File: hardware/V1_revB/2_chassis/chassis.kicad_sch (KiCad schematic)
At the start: 18 parts, among them SW3 NKK_NR01

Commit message: Feat(Hw):Modify_footprint_Chasis_Pot
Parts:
- removed RV3: R_POT_TRIM_US, Global_Library:POT_ECU, symbol Device:R_POT_TRIM_US
- added RV1: R_Potentiometer, RAMN_New_Footprint:New_Pot, symbol Device:R_Potentiometer
- J7, SW2: value ~ -> (none)
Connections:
- net 3V3_ECU: now also RV1.3
- net GND: now also RV1.1
- net Wheel: now also RV1.2

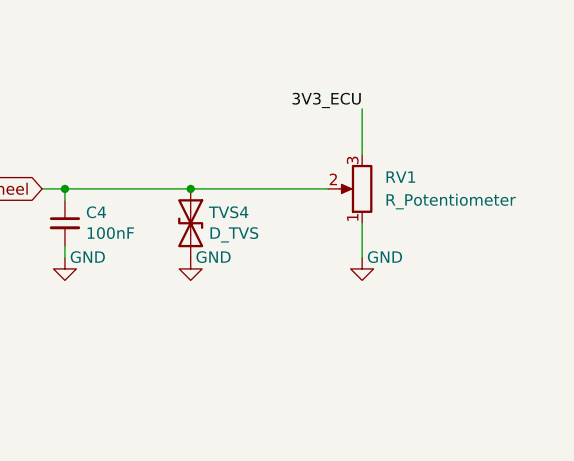
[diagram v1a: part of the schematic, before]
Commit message: Feat(Hw):Modify_BOM_LCSC#
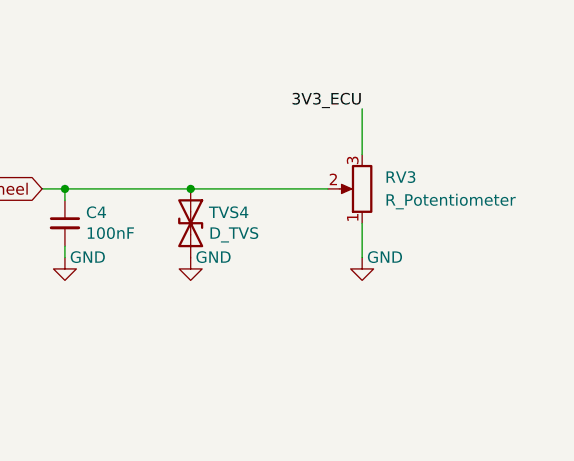
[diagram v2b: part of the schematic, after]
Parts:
- C4: LCSC (none) -> C282519
- J7: LCSC (none) -> C2897414
- R10, R11, R7, R8, R9: LCSC (none) -> C73809
- RV3: renamed from RV1; LCSC (none) -> C6139964
- SW2: LCSC (none) -> C226259
- SW3: LCSC (none) -> C7250022
- TVS4, TVS5, TVS6: LCSC (none) -> C1849694
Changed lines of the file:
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@@
+			)
+		)
+		(property "LCSC" "C226259"
+			(at 128.27 160.02 0)
+			(hide yes)
+			(show_name no)
+			(do_not_autoplace no)
+			(effects
+				(font
+					(size 1.27 1.27)
+				)
 			)
 		)
@@
 			)
 		)
+		(property "LCSC" "C2897414"
+			(at 93.98 68.58 0)
+			(hide yes)
+			(show_name no)
+			(do_not_autoplace no)
+			(effects
+				(font
+					(size 1.27 1.27)
+				)
+			)
+		)
 		(pin "10"
 		)
@@
 		(property "Reference" "SW3"
 			(at 113.03 104.775 0)
-			(show_name no)
+			(show_name yes)
 			(do_not_autoplace no)
 			(effects
@@
 			)
 		)
-		(property "Datasheet" ""
+		(property "Datasheet" "https://www.lcsc.com/datasheet/C7250022.pdf?spm=wm.sxq.inf.ggs&lcsc_vid=FVIIUAUFR1ZWVAJSRgQLVgVfRwNWBVwDR1VbBFNeQ1ExVlNeQFFWV1FSQ1FYUDsOAxUeFF5JWBYZEEoKFBINSQcJGk4eFQsCAgIaSgADAwAHC0slRFVdUVZeQllADxALGw%3D%3D"
 			(at 112.395 113.665 0)
 			(hide yes)
@@
 		)
 		(property "Description" ""
+			(at 113.03 114.3 0)
+			(hide yes)
+			(show_name no)
+			(do_not_autoplace no)
+			(effects
+				(font
+					(size 1.27 1.27)
+				)
+			)
+		)
+		(property "LCSC" "C7250022"
 			(at 113.03 114.3 0)
 			(hide yes)
@@
 			)
 		)
+		(property "LCSC" ""
+			(at 26.67 44.45 0)
+			(hide yes)
+			(show_name no)
+			(do_not_autoplace no)
+			(effects
+				(font
+					(size 1.27 1.27)
+				)
+			)
+		)
 		(instances
 			(project "chassis"
@@
 			)
 		)
+		(property "LCSC" "C73809"
+			(at 96.52 105.41 0)
+			(hide yes)
+			(show_name no)
+			(do_not_autoplace no)
+			(effects
+				(font
+					(size 1.27 1.27)
+				)
+			)
+		)
 		(pin "1"
 		)
@@
 			)
 		)
+		(property "LCSC" "C73809"
+			(at 96.52 114.3 0)
+			(hide yes)
+			(show_name no)
+			(do_not_autoplace no)
+			(effects
+				(font
+					(size 1.27 1.27)
+				)
+			)
+		)
 		(pin "2"
 		)
@@
 			)
 		)
+		(property "LCSC" "C73809"
+			(at 96.52 120.65 0)
+			(hide yes)
+			(show_name no)
+			(do_not_autoplace no)
+			(effects
+				(font
+					(size 1.27 1.27)
+				)
+			)
+		)
 		(pin "2"
 		)
@@
 			)
 		)
+		(property "LCSC" "C73809"
+			(at 96.52 128.27 0)
+			(hide yes)
+			(show_name no)
+			(do_not_autoplace no)
+			(effects
+				(font
+					(size 1.27 1.27)
+				)
+			)
+		)
 		(pin "2"
 		)
@@
 			)
 		)
+		(property "LCSC" "C73809"
+			(at 119.38 154.94 0)
+			(hide yes)
+			(show_name no)
+			(do_not_autoplace no)
+			(effects
+				(font
+					(size 1.27 1.27)
+				)
+			)
+		)
 		(pin "1"
 		)
@@
 			)
 		)
+		(property "LCSC" ""
+			(at 26.67 39.37 0)
+			(hide yes)
+			(show_name no)
+			(do_not_autoplace no)
+			(effects
+				(font
+					(size 1.27 1.27)
+				)
+			)
+		)
 		(instances
 			(project "chassis"
@@
 			)
 		)
+		(property "LCSC" "C282519"
+			(at 137.16 59.69 0)
+			(hide yes)
+			(show_name no)
+			(do_not_autoplace no)
+			(effects
+				(font
+					(size 1.27 1.27)
+				)
+			)
+		)
 		(pin "1"
 		)
@@
 			)
 		)
+		(property "LCSC" "C1849694"
+			(at 151.13 59.69 90)
+			(hide yes)
+			(show_name no)
+			(do_not_autoplace no)
+			(effects
+				(font
+					(size 1.27 1.27)
+				)
+			)
+		)
 		(pin "1"
 		)
@@
 			)
 		)
+		(property "LCSC" "C1849694"
+			(at 130.81 119.38 90)
+			(hide yes)
+			(show_name no)
+			(do_not_autoplace no)
+			(effects
+				(font
+					(size 1.27 1.27)
+				)
+			)
+		)
 		(pin "2"
 		)
@@
 			)
 		)
+		(property "LCSC" "C1849694"
+			(at 115.57 165.1 90)
+			(hide yes)
+			(show_name no)
+			(do_not_autoplace no)
+			(effects
+				(font
+					(size 1.27 1.27)
+				)
+			)
+		)
 		(pin "1"
 		)
@@
 			)
 		)
+		(property "LCSC" ""
+			(at 25.4 176.53 0)
+			(hide yes)
+			(show_name no)
+			(do_not_autoplace no)
+			(effects
+				(font
+					(size 1.27 1.27)
+				)
+			)
+		)
 		(instances
 			(project "chassis"
@@
 			)
 		)
+		(property "LCSC" ""
+			(at 41.91 176.53 0)
+			(hide yes)
+			(show_name no)
+			(do_not_autoplace no)
+			(effects
+				(font
+					(size 1.27 1.27)
+				)
+			)
+		)
 		(instances
 			(project "chassis"
@@
 			)
 		)
+		(property "LCSC" ""
+			(at 58.42 176.53 0)
+			(hide yes)
+			(show_name no)
+			(do_not_autoplace no)
+			(effects
+				(font
+					(size 1.27 1.27)
+				)
+			)
+		)
 		(instances
 			(project "chassis"
@@
 		(in_pos_files yes)
 		(dnp no)
-		(property "Reference" "RV1"
+		(property "Reference" "RV3"
 			(at 172.72 54.6099 0)
 			(show_name no)
@@
 			)
 		)
+		(property "LCSC" "C6139964"
+			(at 170.18 55.88 0)
+			(hide yes)
+			(show_name no)
+			(do_not_autoplace no)
+			(effects
+				(font
+					(size 1.27 1.27)
+				)
+			)
+		)
 		(pin "2"
 		)
@@
 			(project "chassis"
 				(path "/e002719d-0ac0-46ab-ae27-c279a7634c07"
-					(reference "RV1")
-					(unit 1)
-				)
+					(reference "RV3")
+					(unit 1)
+				)

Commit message: Feat(Hw): Modify_and_fix_footprints_and_symbols
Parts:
- removed SW3: NKK_NR01, Akiyuki_UI:NR01, symbol Akiyuki_UI:NKK_NR01
- added SW1: (no value), RAMN_New_Footprint:NR01, symbol RAMN_New_Symbols:SW3
- FID1, FID2, FID3, H3, H4: now not fitted
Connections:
- net 3V3_ECU: now also SW1.1 (3V3)
- net GND: now also SW1.5 (GND)
- net Lamp: now also SW1.3 (Lamp)
- net at R7.2, R8.1: now also SW1.2 (A)
- net at R8.2, R9.1: now also SW1.4 (B)
- net at R10.1, R9.2: now also SW1.6 (C)
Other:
- moved on the sheet: TVS5

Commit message: Feat(Hw): EnhanceComponentLibraries
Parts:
- SW3: renamed from SW1; LCSC (none) -> C7250022
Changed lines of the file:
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@@
 		(in_pos_files yes)
 		(dnp no)
-		(property "Reference" "SW1"
+		(property "Reference" "SW3"
 			(at 116.84 107.95 0)
 			(show_name no)
@@
 			)
 		)
+		(property "LCSC" "C7250022"
+			(at 116.84 116.84 0)
+			(hide yes)
+			(show_name no)
+			(do_not_autoplace no)
+			(effects
+				(font
+					(size 1.27 1.27)
+				)
+			)
+		)
 		(pin "2"
 		)
@@
 			(project "chassis"
 				(path "/e002719d-0ac0-46ab-ae27-c279a7634c07"
-					(reference "SW1")
+					(reference "SW3")
 					(unit 1)
 				)

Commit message: Feat(Hw): UpdateKiCadProjectAndStandardizeComponentProperties
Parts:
- C4: Category (none) -> Electronic Components / Capacitors; LCSC C282519 -> (none); lcsc# (none) -> C282519; manf# (none) -> TCC0603X7R104K500CT
- FID1, FID2, FID3: Category (none) -> Electronic Components / Other Components
- H3, H4: Category (none) -> Production & Packaging / Screws & Hardware
- J7: value (none) -> ~; Category (none) -> Electronic Components / Connectors; LCSC C2897414 -> (none); lcsc# (none) -> C2897414; manf# (none) -> PM254-2-13-Z-8.5
- R10, R11, R7, R8, R9: Category (none) -> Electronic Components / Resistors; LCSC C73809 -> (none); lcsc# (none) -> C73809; manf# (none) -> RS-03K103JT
- RV3: Category (none) -> Electronic Components / Resistors; LCSC C6139964 -> (none); lcsc# (none) -> C6139964; manf# (none) -> P120K-Y20BR50K
- SW2: value (none) -> ~; Category (none) -> Electronic Components / Switches; LCSC C226259 -> (none); lcsc# (none) -> C226259; manf# (none) -> OS102011MA1QN1
- SW3: value (none) -> ~; Category (none) -> Electronic Components / Switches; LCSC C7250022 -> (none); lcsc# (none) -> C7250022; manf# (none) -> NR01104ANG13-2A
- TVS4, TVS5, TVS6: Category (none) -> Electronic Components / Other Components; LCSC C1849694 -> (none); lcsc# (none) -> C1849694; manf# (none) -> SMF5V0TR
